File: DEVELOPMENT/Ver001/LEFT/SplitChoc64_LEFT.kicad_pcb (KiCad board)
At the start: 2 copper layers, 147.3 x 96.8 mm, 68 parts, among them J1 BM02B-SRSS-TB, J3 3V3 GND X Y SW SDA SCL, U1 XIAO nRF52840 Plus

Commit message: Stage parallel trackball FFC connectors in Ver001
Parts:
- added J5: FH19C-6S-0.5SH(10), SplitChoc64_FFC:FH19C-6S-0.5SH_HandSolder, B.Cu at (118.5, 112.8)
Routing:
- net L_GND: track 140.9 -> 155.0 mm
- net L_3V3: track 137.6 -> 142.0 mm
- net L_JOY_SDA: track 123.0 -> 127.0 mm, vias 1 -> 2
- net L_JOY_SW: track 131.6 -> 133.4 mm, vias 1 -> 2
- net L_JOY_Y: track 135.3 -> 136.6 mm, vias 1 -> 2
- net L_JOY_X: track 135.6 -> 136.3 mm, vias 1 -> 2

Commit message: Repair parallel FFC fanout and publish DRC pass 2
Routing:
- net L_JOY_SW: track 133.4 -> 142.1 mm, vias 2 -> 1
- net L_JOY_Y: track 136.6 -> 145.0 mm, vias 2 -> 1
- net L_JOY_X: track 136.3 -> 144.5 mm, vias 2 -> 1
- net L_JOY_SDA: track 127.0 -> 134.2 mm, vias 2 -> 1
- net L_GND: track 155.0 -> 149.0 mm
- net L_3V3: track 142.0 -> 143.3 mm
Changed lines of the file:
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@@
 	(segment
 		(start 122.75 115.85)
-		(end 122.0 116.3)
-		(width 0.15)
-		(layer "B.Cu")
-		(net 18)
-	)
-	(segment
-		(start 122.0 116.3)
-		(end 121.5 116.3)
-		(width 0.15)
-		(layer "B.Cu")
-		(net 18)
-	)
-	(segment
-		(start 121.5 116.3)
-		(end 121.5 113.0)
-		(width 0.15)
-		(layer "B.Cu")
-		(net 18)
-	)
-	(segment
-		(start 121.5 113.0)
-		(end 130.91 113.0)
+		(end 130.91 116.0)
 		(width 0.15)
 		(layer "B.Cu")
@@
 	(segment
 		(start 123.25 115.85)
-		(end 123.3 115.35)
+		(end 132.18 116.0)
 		(width 0.15)
 		(layer "B.Cu")
 		(net 12)
 	)
-	(via
-		(at 123.3 115.35)
-		(size 0.45)
-		(drill 0.2)
-		(layers "F.Cu" "B.Cu")
-		(net 12)
-	)
-	(segment
-		(start 123.3 115.35)
-		(end 123.3 115.5474)
-		(width 0.15)
-		(layer "F.Cu")
-		(net 12)
-	)
 	(segment
 		(start 123.75 115.85)
-		(end 123.9 114.85)
+		(end 133.45 116.0)
 		(width 0.15)
 		(layer "B.Cu")
 		(net 13)
 	)
-	(via
-		(at 123.9 114.85)
-		(size 0.45)
-		(drill 0.2)
-		(layers "F.Cu" "B.Cu")
-		(net 13)
-	)
-	(segment
-		(start 123.9 114.85)
-		(end 123.9 115.0957)
-		(width 0.15)
-		(layer "F.Cu")
-		(net 13)
-	)
 	(segment
 		(start 124.25 115.85)
-		(end 124.5 114.35)
+		(end 134.72 116.0)
 		(width 0.15)
 		(layer "B.Cu")
 		(net 14)
 	)
-	(via
-		(at 124.5 114.35)
-		(size 0.45)
-		(drill 0.2)
-		(layers "F.Cu" "B.Cu")
-		(net 14)
-	)
-	(segment
-		(start 124.5 114.35)
-		(end 124.5 114.6199)
-		(width 0.15)
-		(layer "F.Cu")
-		(net 14)
-	)
 	(segment
 		(start 124.75 115.85)
-		(end 125.1 113.85)
+		(end 135.99 116.0)
 		(width 0.15)
 		(layer "B.Cu")
 		(net 15)
 	)
-	(via
-		(at 125.1 113.85)
-		(size 0.45)
-		(drill 0.2)
-		(layers "F.Cu" "B.Cu")
-		(net 15)
+	(segment
+		(start 125.25 115.85)
+		(end 125.25 116.6)
+		(width 0.15)
+		(layer "B.Cu")
+		(net 17)
 	)
 	(segment
-		(start 125.1 113.85)
-		(end 126.6 113.85)
+		(start 125.25 116.6)
+		(end 129.64 116.6)
 		(width 0.15)
-		(layer "F.Cu")
-		(net 15)
+		(layer "B.Cu")
+		(net 17)
 	)
 	(segment
-		(start 126.6 113.85)
-		(end 126.6 114.3182)
-		(width 0.15)
-		(layer "F.Cu")
-		(net 15)
-	)
-	(segment
-		(start 125.25 115.85)
-		(end 129.64 115.5)
+		(start 129.64 116.6)
+		(end 129.64 116.0)
 		(width 0.15)
 		(layer "B.Cu")

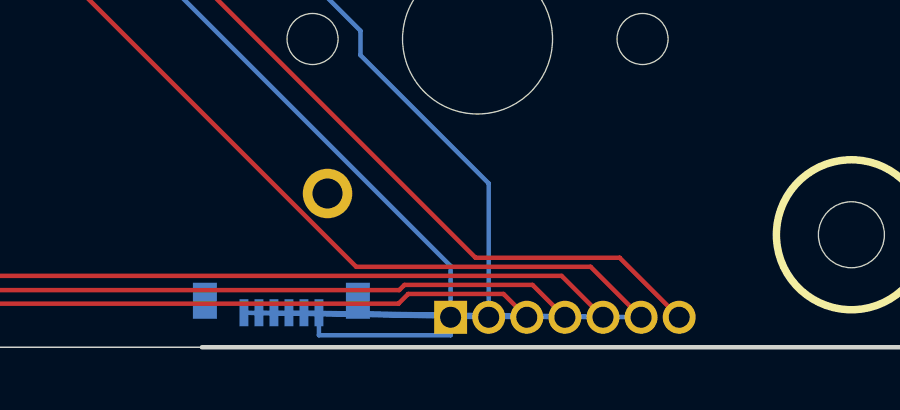
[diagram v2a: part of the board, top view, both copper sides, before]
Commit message: Repair parallel FFC direct fanout
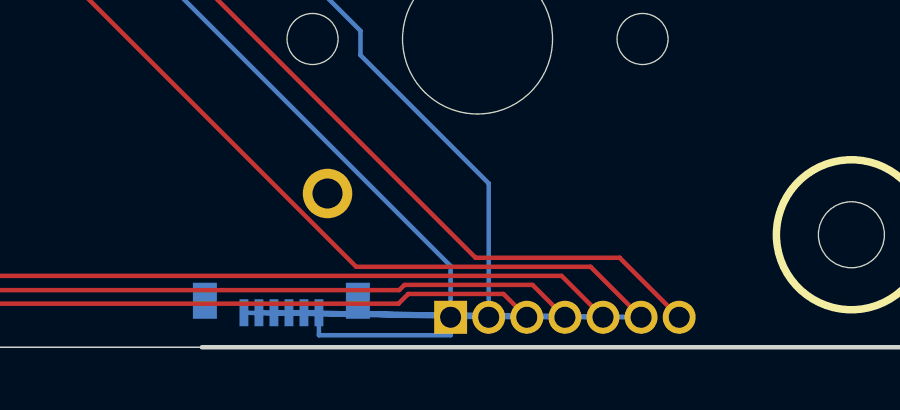
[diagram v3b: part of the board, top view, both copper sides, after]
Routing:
- net L_JOY_SDA: track 134.2 -> 145.5 mm
- net L_JOY_SW: track 142.1 -> 152.6 mm
- net L_JOY_Y: track 145.0 -> 154.7 mm
- net L_JOY_X: track 144.5 -> 153.5 mm
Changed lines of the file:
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@@
+	)
+	(segment
+		(start 123.25 115.85)
+		(end 132.18 116.0)
+		(width 0.15)
+		(layer "B.Cu")
+		(net 12)
+	)
+	(segment
+		(start 123.75 115.85)
+		(end 133.45 116.0)
+		(width 0.15)
+		(layer "B.Cu")
+		(net 13)
+	)
+	(segment
+		(start 124.25 115.85)
+		(end 134.72 116.0)
+		(width 0.15)
+		(layer "B.Cu")
+		(net 14)
+	)
+	(segment
+		(start 124.75 115.85)
+		(end 135.99 116.0)
+		(width 0.15)
+		(layer "B.Cu")
+		(net 15)
 	)
 	(segment

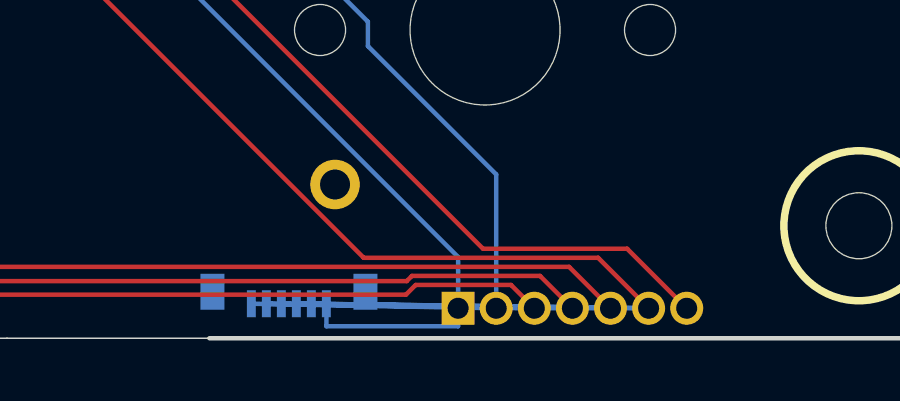
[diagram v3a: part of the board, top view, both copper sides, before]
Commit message: Rebuild clean Ver001 FFC footprint placement and DRC
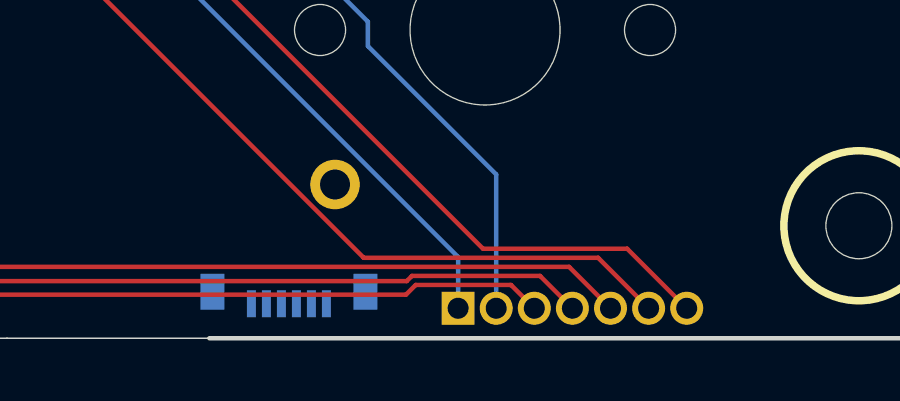
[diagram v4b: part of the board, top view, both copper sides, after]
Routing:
- net L_JOY_SDA: track 145.5 -> 123.0 mm
- net L_JOY_SW: track 152.6 -> 131.6 mm
- net L_JOY_Y: track 154.7 -> 135.3 mm
- net L_JOY_X: track 153.5 -> 135.6 mm
- net L_GND: track 149.0 -> 140.9 mm
- net L_3V3: track 143.3 -> 137.6 mm
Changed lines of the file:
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@@
 		(net 51)
-	)
-	(segment
-		(start 123.25 115.85)
-		(end 132.18 116.0)
-		(width 0.15)
-		(layer "B.Cu")
-		(net 12)
-	)
-	(segment
-		(start 123.75 115.85)
-		(end 133.45 116.0)
-		(width 0.15)
-		(layer "B.Cu")
-		(net 13)
-	)
-	(segment
-		(start 124.25 115.85)
-		(end 134.72 116.0)
-		(width 0.15)
-		(layer "B.Cu")
-		(net 14)
-	)
-	(segment
-		(start 124.75 115.85)
-		(end 135.99 116.0)
-		(width 0.15)
-		(layer "B.Cu")
-		(net 15)
-	)
-	(segment
-		(start 122.75 115.85)
-		(end 130.91 116.0)
-		(width 0.15)
-		(layer "B.Cu")
-		(net 18)
-	)
-	(segment
-		(start 123.25 115.85)
-		(end 132.18 116.0)
-		(width 0.15)
-		(layer "B.Cu")
-		(net 12)
-	)
-	(segment
-		(start 123.75 115.85)
-		(end 133.45 116.0)
-		(width 0.15)
-		(layer "B.Cu")
-		(net 13)
-	)
-	(segment
-		(start 124.25 115.85)
-		(end 134.72 116.0)
-		(width 0.15)
-		(layer "B.Cu")
-		(net 14)
-	)
-	(segment
-		(start 124.75 115.85)
-		(end 135.99 116.0)
-		(width 0.15)
-		(layer "B.Cu")
-		(net 15)
-	)
-	(segment
-		(start 125.25 115.85)
-		(end 125.25 116.6)
-		(width 0.15)
-		(layer "B.Cu")
-		(net 17)
-	)
-	(segment
-		(start 125.25 116.6)
-		(end 129.64 116.6)
-		(width 0.15)
-		(layer "B.Cu")
-		(net 17)
-	)
-	(segment
-		(start 129.64 116.6)
-		(end 129.64 116.0)
-		(width 0.15)
-		(layer "B.Cu")
-		(net 17)
 	)
 	(embedded_fonts no)

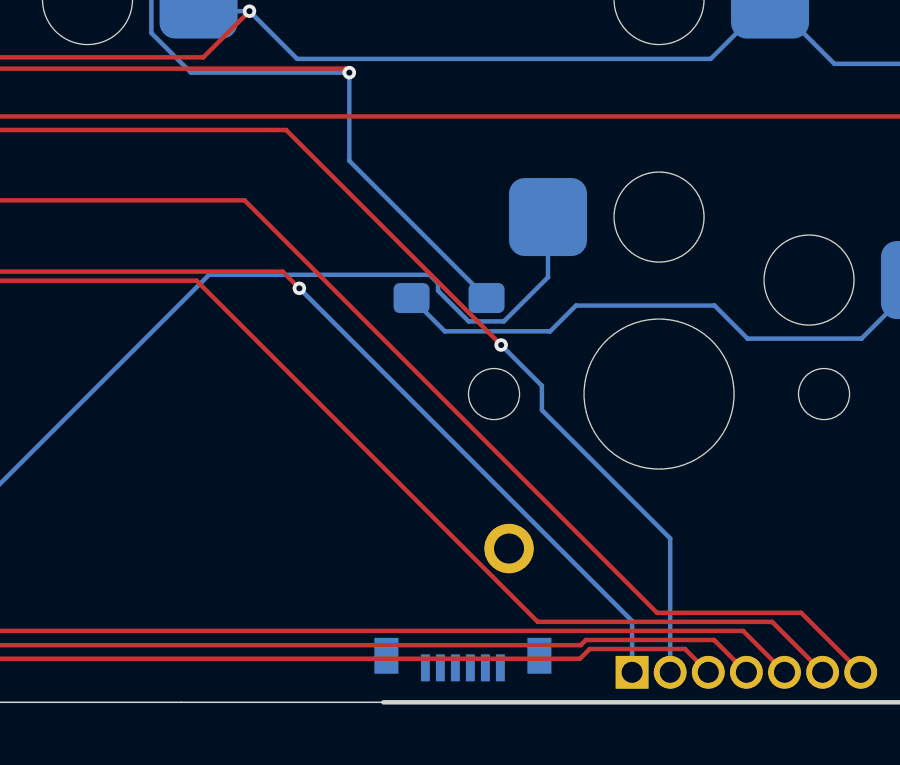
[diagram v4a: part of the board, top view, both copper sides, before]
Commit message: Route Ver001 FFC power nets and publish DRC
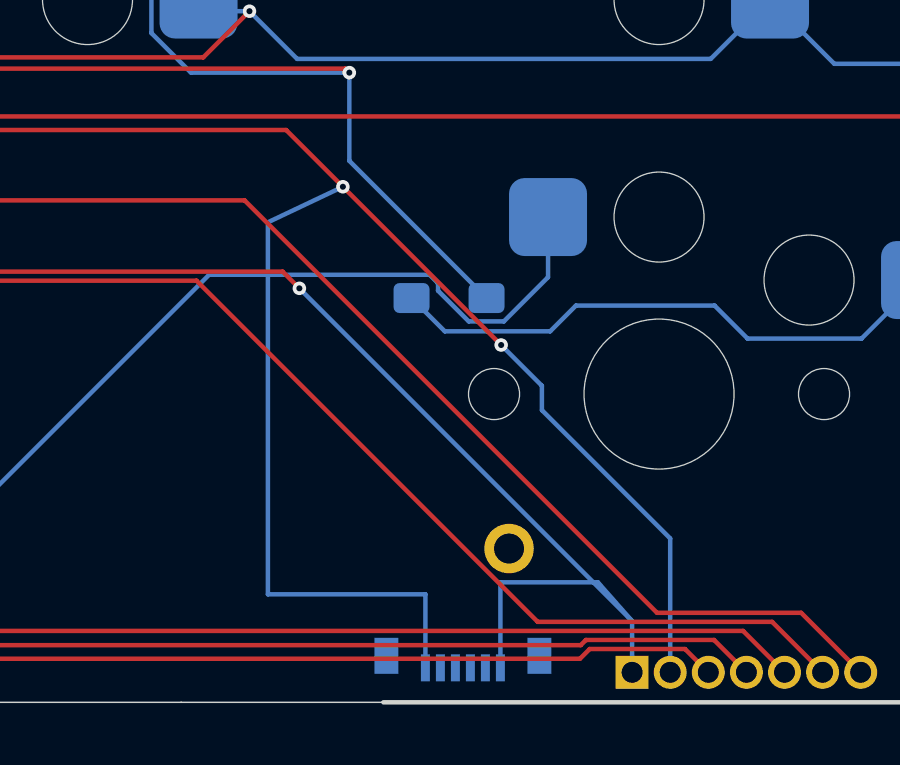
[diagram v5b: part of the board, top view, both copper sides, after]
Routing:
- net L_GND: track 140.9 -> 163.8 mm, vias 3 -> 4
- net L_3V3: track 137.6 -> 145.4 mm
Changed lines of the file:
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@@
 		(net 51)
+	)
+	(segment
+		(start 125.25 115.85)
+		(end 125.25 113.0)
+		(width 0.15)
+		(layer "B.Cu")
+		(net 17)
+	)
+	(segment
+		(start 125.25 113.0)
+		(end 128.5 113.0)
+		(width 0.15)
+		(layer "B.Cu")
+		(net 17)
+	)
+	(segment
+		(start 128.5 113.0)
+		(end 129.64 114.2915)
+		(width 0.15)
+		(layer "B.Cu")
+		(net 17)
+	)
+	(segment
+		(start 122.75 115.85)
+		(end 122.75 113.4)
+		(width 0.15)
+		(layer "B.Cu")
+		(net 18)
+	)
+	(segment
+		(start 122.75 113.4)
+		(end 117.5 113.4)
+		(width 0.15)
+		(layer "B.Cu")
+		(net 18)
+	)
+	(segment
+		(start 117.5 113.4)
+		(end 117.5 101.0)
+		(width 0.15)
+		(layer "B.Cu")
+		(net 18)
+	)
+	(segment
+		(start 117.5 101.0)
+		(end 120.0 99.8147)
+		(width 0.15)
+		(layer "B.Cu")
+		(net 18)
+	)
+	(via
+		(at 120.0 99.8147)
+		(size 0.45)
+		(drill 0.2)
+		(layers "F.Cu" "B.Cu")
+		(net 18)
 	)
 	(embedded_fonts no)

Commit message: Restore un-routed FFC footprints for Freerouting
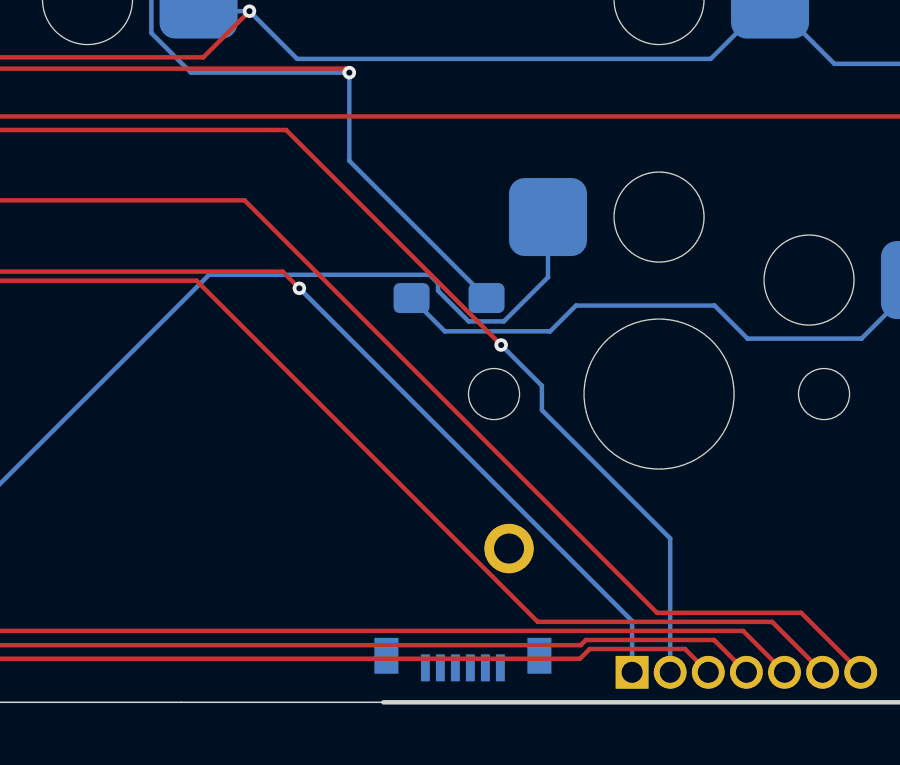
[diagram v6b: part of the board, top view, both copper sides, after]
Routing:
- net L_GND: track 163.8 -> 140.9 mm, vias 4 -> 3
- net L_3V3: track 145.4 -> 137.6 mm
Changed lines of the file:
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@@
 		(net 51)
-	)
-	(segment
-		(start 125.25 115.85)
-		(end 125.25 113.0)
-		(width 0.15)
-		(layer "B.Cu")
-		(net 17)
-	)
-	(segment
-		(start 125.25 113.0)
-		(end 128.5 113.0)
-		(width 0.15)
-		(layer "B.Cu")
-		(net 17)
-	)
-	(segment
-		(start 128.5 113.0)
-		(end 129.64 114.2915)
-		(width 0.15)
-		(layer "B.Cu")
-		(net 17)
-	)
-	(segment
-		(start 122.75 115.85)
-		(end 122.75 113.4)
-		(width 0.15)
-		(layer "B.Cu")
-		(net 18)
-	)
-	(segment
-		(start 122.75 113.4)
-		(end 117.5 113.4)
-		(width 0.15)
-		(layer "B.Cu")
-		(net 18)
-	)
-	(segment
-		(start 117.5 113.4)
-		(end 117.5 101.0)
-		(width 0.15)
-		(layer "B.Cu")
-		(net 18)
-	)
-	(segment
-		(start 117.5 101.0)
-		(end 120.0 99.8147)
-		(width 0.15)
-		(layer "B.Cu")
-		(net 18)
-	)
-	(via
-		(at 120.0 99.8147)
-		(size 0.45)
-		(drill 0.2)
-		(layers "F.Cu" "B.Cu")
-		(net 18)
 	)
 	(embedded_fonts no)
